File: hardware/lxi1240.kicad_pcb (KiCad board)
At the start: 2 copper layers, 105.4 x 62.2 mm, 6 parts, among them J1 1240COMM, J2 1240COMM_EXT

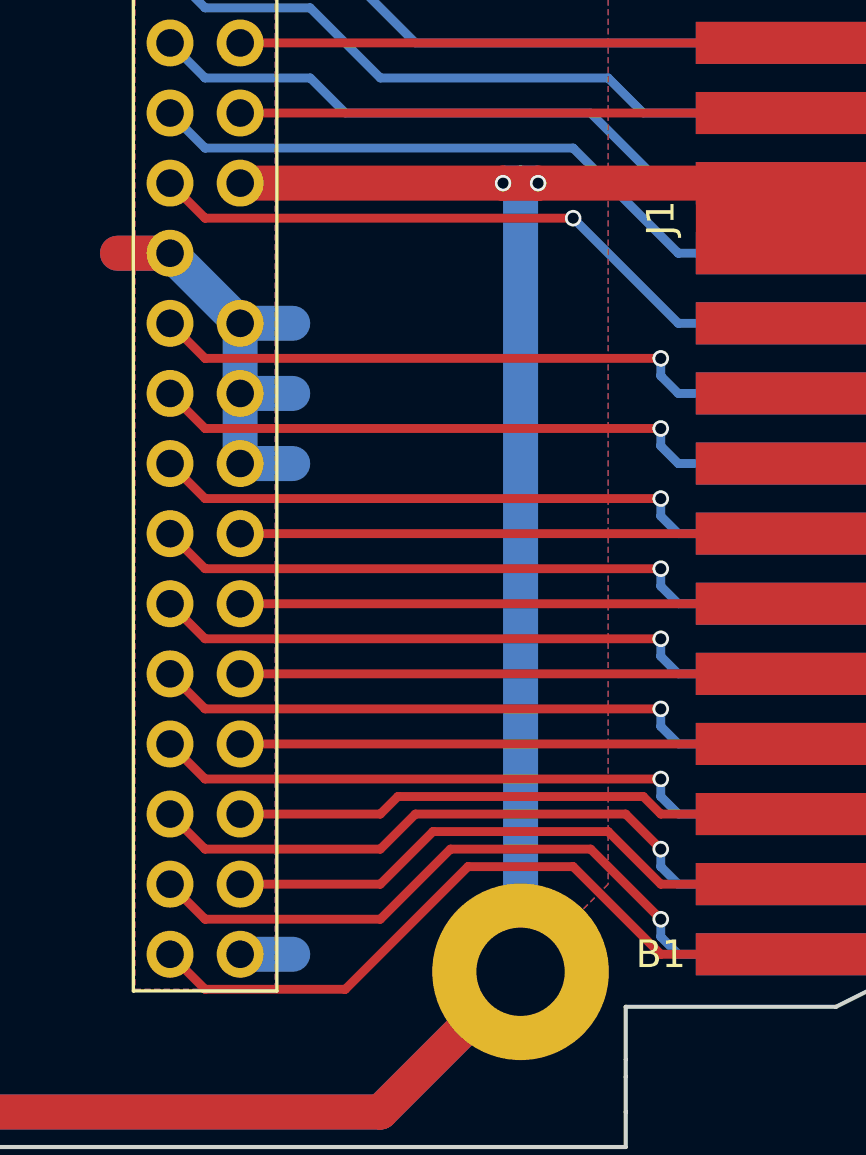
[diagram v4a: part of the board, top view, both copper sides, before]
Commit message: Move PE to ATA pin 28 so slave connector is usable.
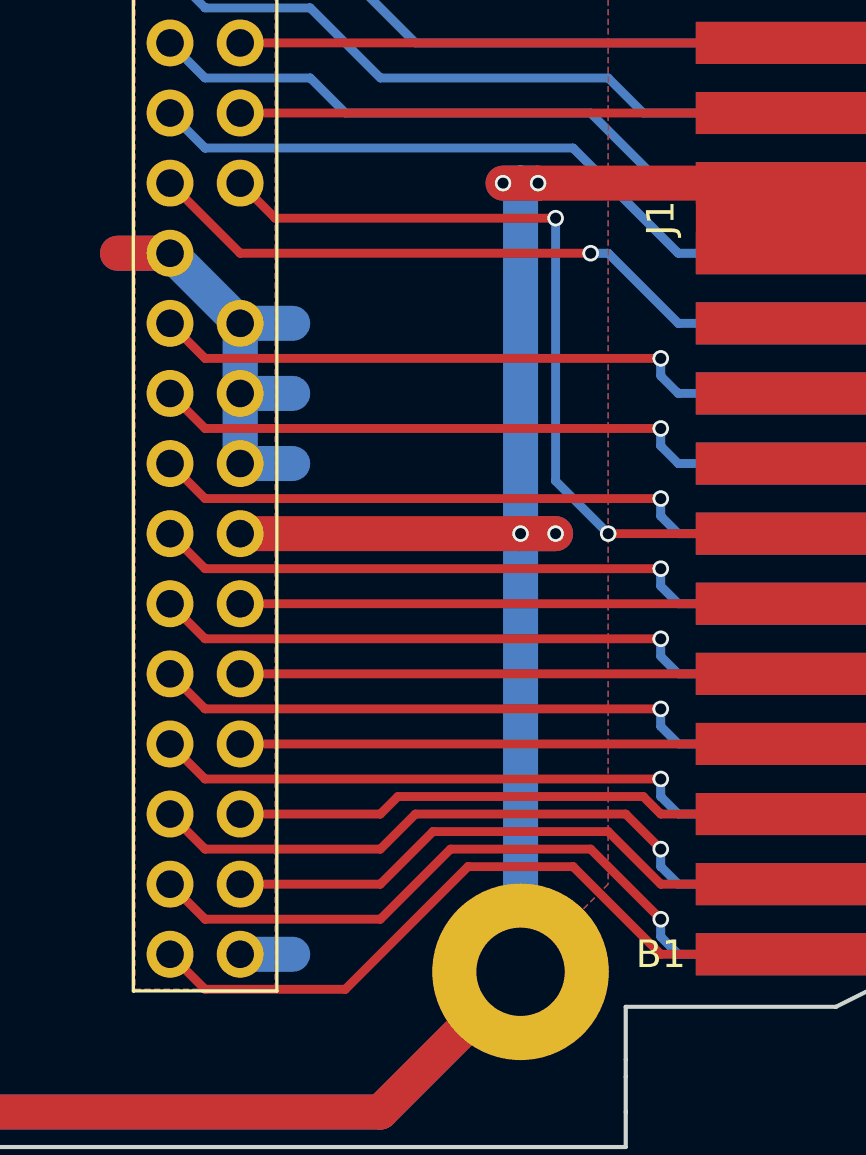
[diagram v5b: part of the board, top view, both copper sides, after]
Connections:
- J2 pad 18: Earth_Protective -> /H-A13
- J2 pad 28: /H-A13 -> Earth_Protective
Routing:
- net /H-A13: track 16.5 -> 27.4 mm, vias 0 -> 2
- net Earth_Protective: track 514.0 -> 517.2 mm, vias 2 -> 4
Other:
- board text added: "SOCKET EXTENDER USE 80-CONDUCTOR ATA RIBBON"
- board text removed: "USE 80-CONDUCTOR ATA RIBBON DO NOT USE SLAVE CONNECTOR"
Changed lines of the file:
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@@
     (thickness 1.6)
     (drawings 63)
-    (tracks 212)
+    (tracks 224)
     (zones 0)
     (modules 6)
@@
     (pad_to_mask_clearance 0.2)
     (aux_axis_origin 0 0)
-    (visible_elements FFFEEF7F)
+    (visible_elements FFFEEB7F)
     (pcbplotparams
       (layerselection 0x00030_80000001)
@@
       (net 29 /H-D2))
     (pad 18 thru_hole oval (at 2.54 20.32) (size 1.7 1.7) (drill 1) (layers *.Cu *.Mask)
-      (net 3 Earth_Protective))
+      (net 13 /H-A13))
     (pad 19 thru_hole oval (at 0 22.86) (size 1.7 1.7) (drill 1) (layers *.Cu *.Mask)
       (net 1 GND))
@@
       (net 25 /H-D5))
     (pad 28 thru_hole oval (at 2.54 33.02) (size 1.7 1.7) (drill 1) (layers *.Cu *.Mask)
-      (net 13 /H-A13))
+      (net 3 Earth_Protective))
     (pad 29 thru_hole oval (at 0 35.56) (size 1.7 1.7) (drill 1) (layers *.Cu *.Mask)
       (net 24 /H-D3))
@@
     )
   )
-  (gr_text "USE 80-CONDUCTOR ATA RIBBON\nDO NOT USE SLAVE CONNECTOR" (at 210.185 88.9 270) (layer B.SilkS)
+  (gr_text "SOCKET EXTENDER\nUSE 80-CONDUCTOR ATA RIBBON" (at 210.185 88.9 270) (layer B.SilkS)
     (effects (font (size 1.5 1.5) (thickness 0.3)) (justify mirror))
   )
@@
     (effects (font (size 1.5 1.5) (thickness 0.3)) (justify right mirror))
   )
-  (gr_text A13 (at 202.565 97.79) (layer B.SilkS)
+  (gr_text PE (at 202.565 97.79) (layer B.SilkS)
     (effects (font (size 1.5 1.5) (thickness 0.3)) (justify right mirror))
   )
@@
     (effects (font (size 1.5 1.5) (thickness 0.3)) (justify right mirror))
   )
-  (gr_text PE (at 202.565 85.09) (layer B.SilkS)
+  (gr_text A13 (at 202.565 85.09) (layer B.SilkS)
     (effects (font (size 1.5 1.5) (thickness 0.3)) (justify right mirror))
   )
@@
   (segment (start 216.535 67.31) (end 213.995 69.85) (width 1.27) (layer F.Cu) (net 2))
   (segment (start 213.995 69.85) (end 213.36 70.485) (width 1.27) (layer F.Cu) (net 2))
+  (segment (start 210.82 97.79) (end 212.09 97.79) (width 1.27) (layer B.Cu) (net 3))
+  (segment (start 210.82 97.79) (end 212.09 97.79) (width 1.27) (layer F.Cu) (net 3))
+  (via (at 212.09 97.79) (size 0.6) (drill 0.4) (layers F.Cu B.Cu) (net 3))
+  (segment (start 200.66 97.79) (end 210.82 97.79) (width 1.27) (layer F.Cu) (net 3))
+  (segment (start 210.82 85.09) (end 210.82 97.79) (width 1.27) (layer B.Cu) (net 3))
+  (segment (start 210.82 97.79) (end 210.82 113.665) (width 1.27) (layer B.Cu) (net 3))
+  (via (at 210.82 97.79) (size 0.6) (drill 0.4) (layers F.Cu B.Cu) (net 3))
   (segment (start 129.54 59.055) (end 205.74 59.055) (width 1.27) (layer B.Cu) (net 3))
   (segment (start 205.74 118.745) (end 129.54 118.745) (width 1.27) (layer B.Cu) (net 3))
@@
   (via (at 210.185 85.09) (size 0.6) (drill 0.4) (layers F.Cu B.Cu) (net 3))
   (segment (start 211.455 85.09) (end 210.82 85.09) (width 1.27) (layer B.Cu) (net 3))
-  (segment (start 210.82 85.09) (end 210.82 113.665) (width 1.27) (layer B.Cu) (net 3))
   (via (at 211.455 85.09) (size 0.6) (drill 0.4) (layers F.Cu B.Cu) (net 3))
   (segment (start 210.185 85.09) (end 211.455 85.09) (width 1.27) (layer F.Cu) (net 3))
   (segment (start 211.455 85.09) (end 217.17 85.09) (width 1.27) (layer F.Cu) (net 3))
-  (segment (start 200.66 85.09) (end 210.185 85.09) (width 1.27) (layer F.Cu) (net 3))
   (segment (start 124.46 113.665) (end 129.54 118.745) (width 1.27) (layer F.Cu) (net 3))
   (segment (start 205.74 118.745) (end 210.82 113.665) (width 1.27) (layer F.Cu) (net 3))
@@
   (segment (start 217.17 80.01) (end 200.66 80.01) (width 0.32258) (layer F.Cu) (net 8))
   (segment (start 217.17 82.55) (end 200.66 82.55) (width 0.32258) (layer F.Cu) (net 9))
-  (segment (start 217.17 97.79) (end 200.66 97.79) (width 0.32258) (layer F.Cu) (net 13))
+  (segment (start 212.09 86.36) (end 201.93 86.36) (width 0.32258) (layer F.Cu) (net 13))
+  (segment (start 201.93 86.36) (end 200.66 85.09) (width 0.32258) (layer F.Cu) (net 13))
+  (segment (start 212.09 95.885) (end 212.09 86.36) (width 0.32258) (layer B.Cu) (net 13))
+  (via (at 212.09 86.36) (size 0.6) (drill 0.4) (layers F.Cu B.Cu) (net 13))
+  (segment (start 213.995 97.79) (end 212.09 95.885) (width 0.32258) (layer B.Cu) (net 13))
+  (segment (start 217.17 97.79) (end 213.995 97.79) (width 0.32258) (layer F.Cu) (net 13))
+  (via (at 213.995 97.79) (size 0.6) (drill 0.4) (layers F.Cu B.Cu) (net 13))
   (segment (start 217.17 100.33) (end 200.66 100.33) (width 0.32258) (layer F.Cu) (net 14))
   (segment (start 217.17 102.87) (end 200.66 102.87) (width 0.32258) (layer F.Cu) (net 15))
@@
   (segment (start 215.9 92.075) (end 215.9 91.44) (width 0.32258) (layer B.Cu) (net 28))
   (segment (start 216.535 92.71) (end 215.9 92.075) (width 0.32258) (layer B.Cu) (net 28))
+  (segment (start 213.36 87.63) (end 213.995 87.63) (width 0.32258) (layer B.Cu) (net 29))
+  (segment (start 213.995 87.63) (end 216.535 90.17) (width 0.32258) (layer B.Cu) (net 29))
+  (segment (start 198.12 85.09) (end 200.66 87.63) (width 0.32258) (layer F.Cu) (net 29))
+  (segment (start 200.66 87.63) (end 213.36 87.63) (width 0.32258) (layer F.Cu) (net 29))
+  (via (at 213.36 87.63) (size 0.6) (drill 0.4) (layers F.Cu B.Cu) (net 29))
   (segment (start 217.17 90.17) (end 216.535 90.17) (width 0.32258) (layer B.Cu) (net 29))
-  (segment (start 216.535 90.17) (end 212.725 86.36) (width 0.32258) (layer B.Cu) (net 29))
-  (via (at 212.725 86.36) (size 0.6) (drill 0.4) (layers F.Cu B.Cu) (net 29))
-  (segment (start 212.725 86.36) (end 199.39 86.36) (width 0.32258) (layer F.Cu) (net 29))
-  (segment (start 199.39 86.36) (end 198.12 85.09) (width 0.32258) (layer F.Cu) (net 29))
   (segment (start 217.17 87.63) (end 216.535 87.63) (width 0.32258) (layer B.Cu) (net 30))
   (segment (start 199.39 83.82) (end 198.12 82.55) (width 0.32258) (layer B.Cu) (net 30))

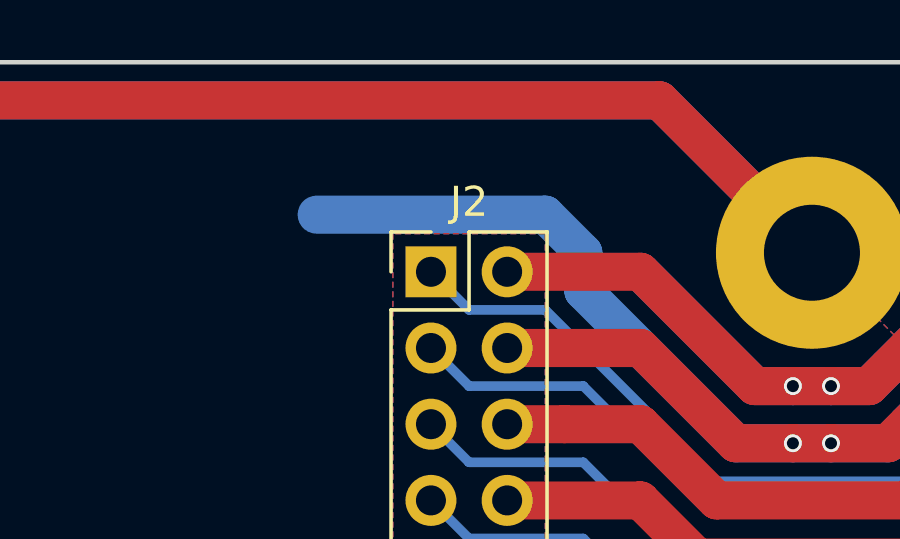
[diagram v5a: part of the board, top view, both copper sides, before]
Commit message: Shorten ground paths.
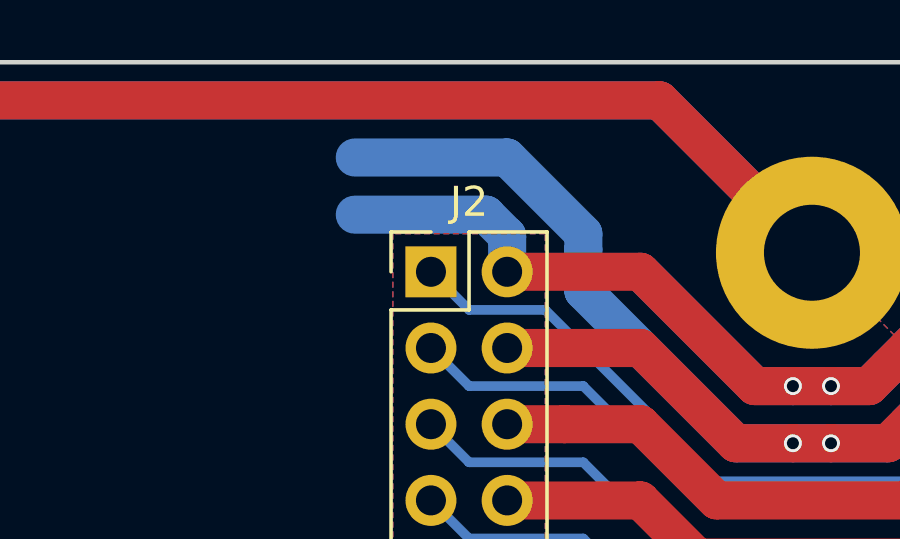
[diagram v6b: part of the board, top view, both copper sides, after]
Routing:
- net GND: track 58.6 -> 65.2 mm
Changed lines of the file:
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@@
     (thickness 1.6)
     (drawings 63)
-    (tracks 224)
+    (tracks 228)
     (zones 0)
     (modules 6)
@@
     (arrow2b (pts (xy 226.06 64.77) (xy 226.646421 65.896504)))
   )
+  (segment (start 199.957081 62.865) (end 195.58 62.865) (width 1.27) (layer B.Cu) (net 1))
+  (segment (start 200.66 64.77) (end 200.66 63.567919) (width 1.27) (layer B.Cu) (net 1))
+  (segment (start 200.66 63.567919) (end 199.957081 62.865) (width 1.27) (layer B.Cu) (net 1))
   (segment (start 200.66 90.17) (end 202.565 90.17) (width 1.27) (layer B.Cu) (net 1))
   (segment (start 200.66 92.71) (end 202.565 92.71) (width 1.27) (layer B.Cu) (net 1))
@@
   (segment (start 216.535 64.77) (end 213.36 67.945) (width 1.27) (layer F.Cu) (net 1))
   (segment (start 213.36 67.945) (end 212.725 68.58) (width 1.27) (layer F.Cu) (net 1))
+  (segment (start 200.66 60.96) (end 195.58 60.96) (width 1.27) (layer B.Cu) (net 2))
+  (segment (start 203.2 63.5) (end 200.66 60.96) (width 1.27) (layer B.Cu) (net 2))
+  (segment (start 203.2 64.029011) (end 203.2 63.5) (width 1.27) (layer B.Cu) (net 2))
+  (segment (start 203.2 65.405) (end 203.2 64.029011) (width 1.27) (layer B.Cu) (net 2))
   (segment (start 210.185 70.485) (end 208.28 70.485) (width 1.27) (layer B.Cu) (net 2))
-  (segment (start 201.93 62.865) (end 194.31 62.865) (width 1.27) (layer B.Cu) (net 2))
-  (segment (start 203.2 64.135) (end 201.93 62.865) (width 1.27) (layer B.Cu) (net 2))
-  (segment (start 203.2 65.405) (end 203.2 64.135) (width 1.27) (layer B.Cu) (net 2))
   (segment (start 208.28 70.485) (end 203.2 65.405) (width 1.27) (layer B.Cu) (net 2))
   (via (at 211.455 70.485) (size 0.6) (drill 0.4) (layers F.Cu B.Cu) (net 2))
